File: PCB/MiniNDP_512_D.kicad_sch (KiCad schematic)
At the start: 17 parts, among them J1 Conn_02x20_Odd_Even, U1 HC138, U2 4040, U3 FCT821, U4 AS6C4008, U5 2G04, U6 1G32

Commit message: make E version default, easier to solder
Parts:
- added N1: MiniNDP_Cover, 000_LOCAL:MiniNDP_Cover, symbol 000_LOCAL:Housing
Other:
- note added: "TANDY 100/102/200 BUS -> Effect (A) ~{YO} A8 A9 A10 -> ~{BLOCK} ~{BYTE} Function L X X X X X X X H X X X X X X X L X X X X H L H L L -> L H Select BLOCK # from BANK 0 H L H L H -> L H Select BLOCK # from BANK 1 H L H H X -> H L Read or Write BYTE ~{BLOCK} L: sets A0-A9 to 0, updates A10-A18 from AD0-AD7 & BUS_A10 H: latches A10-A18 ~{BYTE} L: enables SRAM for read or write H: disables SRAM, incre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"
- note removed: "TANDY 100/102/200 BUS (A) ~{YO} A8 A9 A10 -> ~{BLOCK} ~{BYTE} L X X X X X X X H X X X X X X X L X X X X H L H L L -> L H Select BLOCK # from BANK0 H L H L H -> L H Select BLOCK # from BANK1 H L H H X -> H L READ/WRITE BYTE Each ~{BLOCK} pulse low: sets SRAM A0-A9 to 0 sets SRAM A10-A19 from BUS AD0-AD7 & A10 (AD0-AD7 = block#, BUS_A10 = bank#) On returning high: holds SRAM A10-A19 latched while h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"
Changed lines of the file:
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@@
 		)
 	)
-	(text "TANDY 100/102/200 BUS\n\n(A)	~{YO}   A8   A9  A10  ->  ~{BLOCK} ~{BYTE}\nL	X	X	X	X		X	  X\nX	H	X	X	X		X	  X\nX	X	L	X	X		X	  X\nH	L	H	L	L	->  L	  H  Select BLOCK # from BANK0\nH	L	H	L	H	->  L	  H  Select BLOCK # from BANK1\nH	L	H	H	X	->  H	  L  READ/WRITE BYTE\n\nEach ~{BLOCK} pulse low:\n  sets SRAM A0-A9 to 0\n  sets SRAM A10-A19 from BUS AD0-AD7 & A10\n  (AD0-AD7 = block#, BUS_A10 = bank#)\nOn returning high:\n  holds SRAM A10-A19 latched while high\n\nEach ~{BYTE} pulse low:\n  enables SRAM for read or write while low\nOn returning high:\n  disables SRAM\n  increments SRAM A0-A9 by 1\n"
-		(exclude_from_sim no)
-		(at 16.51 193.548 0)
-		(effects
-			(font
-				(face "KiCad Font")
-				(size 1 1)
-			)
-			(justify left bottom)
-		)
-	)
 	(text "3V"
 		(exclude_from_sim no)
@@
 		)
 	)
+	(text "TANDY 100/102/200 BUS  ->  Effect\n\n(A)	~{YO}   A8   A9  A10  ->  ~{BLOCK} ~{BYTE}    Function\nL	X	X	X	X		X	  X\nX	H	X	X	X		X	  X\nX	X	L	X	X		X	  X\nH	L	H	L	L	->  L	  H  Select BLOCK # from BANK 0\nH	L	H	L	H	->  L	  H  Select BLOCK # from BANK 1\nH	L	H	H	X	->  H	  L  Read or Write BYTE\n\n~{BLOCK}\nL: sets A0-A9 to 0, updates A10-A18 from AD0-AD7 & BUS_A10\nH: latches A10-A18\n\n~{BYTE}\nL: enables SRAM for read or write\nH: disables SRAM, increments A0-A9 by 1\n"
+		(exclude_from_sim no)
+		(at 18.288 191.77 0)
+		(effects
+			(font
+				(face "KiCad Font")
+				(size 1 1)
+			)
+			(justify left bottom)
+		)
+	)
 	(text "BUS_A12"
 		(exclude_from_sim no)
@@
 		)
 	)
-	(label "A2"
-		(at 636.27 17.78 0)
-		(fields_autoplaced yes)
-		(effects
-			(font
-				(size 1.27 1.27)
-			)
-			(justify left bottom)
-		)
-	)
 	(label "~{CE}"
 		(at 247.65 76.2 0)
@@
 		)
 	)
-	(label "A2"
-		(at 843.28 -5.08 0)
-		(fields_autoplaced yes)
-		(effects
-			(font
-				(size 1.27 1.27)
-			)
-			(justify left bottom)
-		)
-	)
 	(label "AD5"
 		(at 247.65 58.42 0)
@@
 		)
 	)
-	(label "A0"
-		(at 636.27 12.7 0)
-		(fields_autoplaced yes)
-		(effects
-			(font
-				(size 1.27 1.27)
-			)
-			(justify left bottom)
-		)
-	)
 	(label "A8"
 		(at 165.1 57.15 0)
@@
 		)
 	)
-	(label "A3"
-		(at 843.28 -2.54 0)
-		(fields_autoplaced yes)
-		(effects
-			(font
-				(size 1.27 1.27)
-			)
-			(justify left bottom)
-		)
-	)
-	(label "A4"
-		(at 604.52 12.7 0)
-		(fields_autoplaced yes)
-		(effects
-			(font
-				(size 1.27 1.27)
-			)
-			(justify left bottom)
-		)
-	)
 	(label "A1"
 		(at 165.1 39.37 0)
@@
 		)
 	)
-	(label "A1"
-		(at 636.27 15.24 0)
-		(fields_autoplaced yes)
-		(effects
-			(font
-				(size 1.27 1.27)
-			)
-			(justify left bottom)
-		)
-	)
 	(label "A4"
 		(at 165.1 46.99 0)
@@
 		)
 	)
-	(label "A6"
-		(at 604.52 17.78 0)
-		(fields_autoplaced yes)
-		(effects
-			(font
-				(size 1.27 1.27)
-			)
-			(justify left bottom)
-		)
-	)
 	(label "A9"
 		(at 165.1 59.69 0)
@@
 		)
 	)
-	(label "A1"
-		(at 843.28 -7.62 0)
-		(fields_autoplaced yes)
-		(effects
-			(font
-				(size 1.27 1.27)
-			)
-			(justify left bottom)
-		)
-	)
-	(label "A3"
-		(at 636.27 20.32 0)
-		(fields_autoplaced yes)
-		(effects
-			(font
-				(size 1.27 1.27)
-			)
-			(justify left bottom)
-		)
-	)
 	(label "AD4"
 		(at 139.7 110.49 180)
@@
 		)
 	)
-	(label "A5"
-		(at 604.52 15.24 0)
-		(fields_autoplaced yes)
-		(effects
-			(font
-				(size 1.27 1.27)
-			)
-			(justify left bottom)
-		)
-	)
 	(label "A3"
 		(at 165.1 44.45 0)
@@
 		)
 	)
-	(label "A7"
-		(at 604.52 20.32 0)
-		(fields_autoplaced yes)
-		(effects
-			(font
-				(size 1.27 1.27)
-			)
-			(justify left bottom)
-		)
-	)
 	(label "{BUS_A[8..9],(A),~{Y0}}"
 		(at 46.99 69.85 0)
@@
 		)
 	)
-	(label "A0"
-		(at 843.28 -10.16 0)
-		(fields_autoplaced yes)
-		(effects
-			(font
-				(size 1.27 1.27)
-			)
-			(justify left bottom)
-		)
-	)
 	(label "AD4"
 		(at 50.8 95.25 180)
@@
 					(unit 1)
 				)
+			)
+		)
+	)
+	(symbol
+		(lib_id "000_LOCAL:Housing")
+		(at 234.95 29.21 0)
+		(unit 1)
+		(exclude_from_sim yes)
+		(in_bom no)
+		(on_board yes)
+		(dnp no)
+		(fields_autoplaced yes)
+		(property "Reference" "N1"
+			(at 238.76 28.2574 0)
+			(effects
+				(font
+					(size 1.27 1.27)
+				)
+				(justify left)
+			)
+		)
+		(property "Value" "MiniNDP_Cover"
+			(at 238.76 30.7974 0)
+			(effects
+				(font
+					(size 1.27 1.27)
+				)
+				(justify left)
+			)
+		)
+		(property "Footprint" "000_LOCAL:MiniNDP_Cover"
+			(at 236.22 27.94 0)
+			(effects
+				(font
+					(size 1.27 1.27)
+				)
+				(hide yes)
+			)
+		)
+		(property "Datasheet" "../COVER/MiniNDP_Cover.scad"
+			(at 236.22 27.94 0)
+			(effects
+				(font
+					(size 1.27 1.27)
+				)
+				(hide yes)
+			)
+		)
+		(property "Description" "Snap cover for MiniNDP"
+			(at 234.95 29.21 0)
+			(effects
+				(font
+					(size 1.27 1.27)
+				)
+				(hide yes)
+			)
+		)
+		(property "MPN" "MiniNDP_Cover.stl"
+			(at 234.95 29.21 0)
+			(effects
+				(font
+					(size 1.27 1.27)
+				)
+				(hide yes)
+			)
+		)
+		(instances
+			(project "MiniNDP_512_D"
+				(path "/f15c2929-5cf4-4b4e-965d-148e1bec8a42"
+					(reference "N1")
+					(unit 1)
+				)

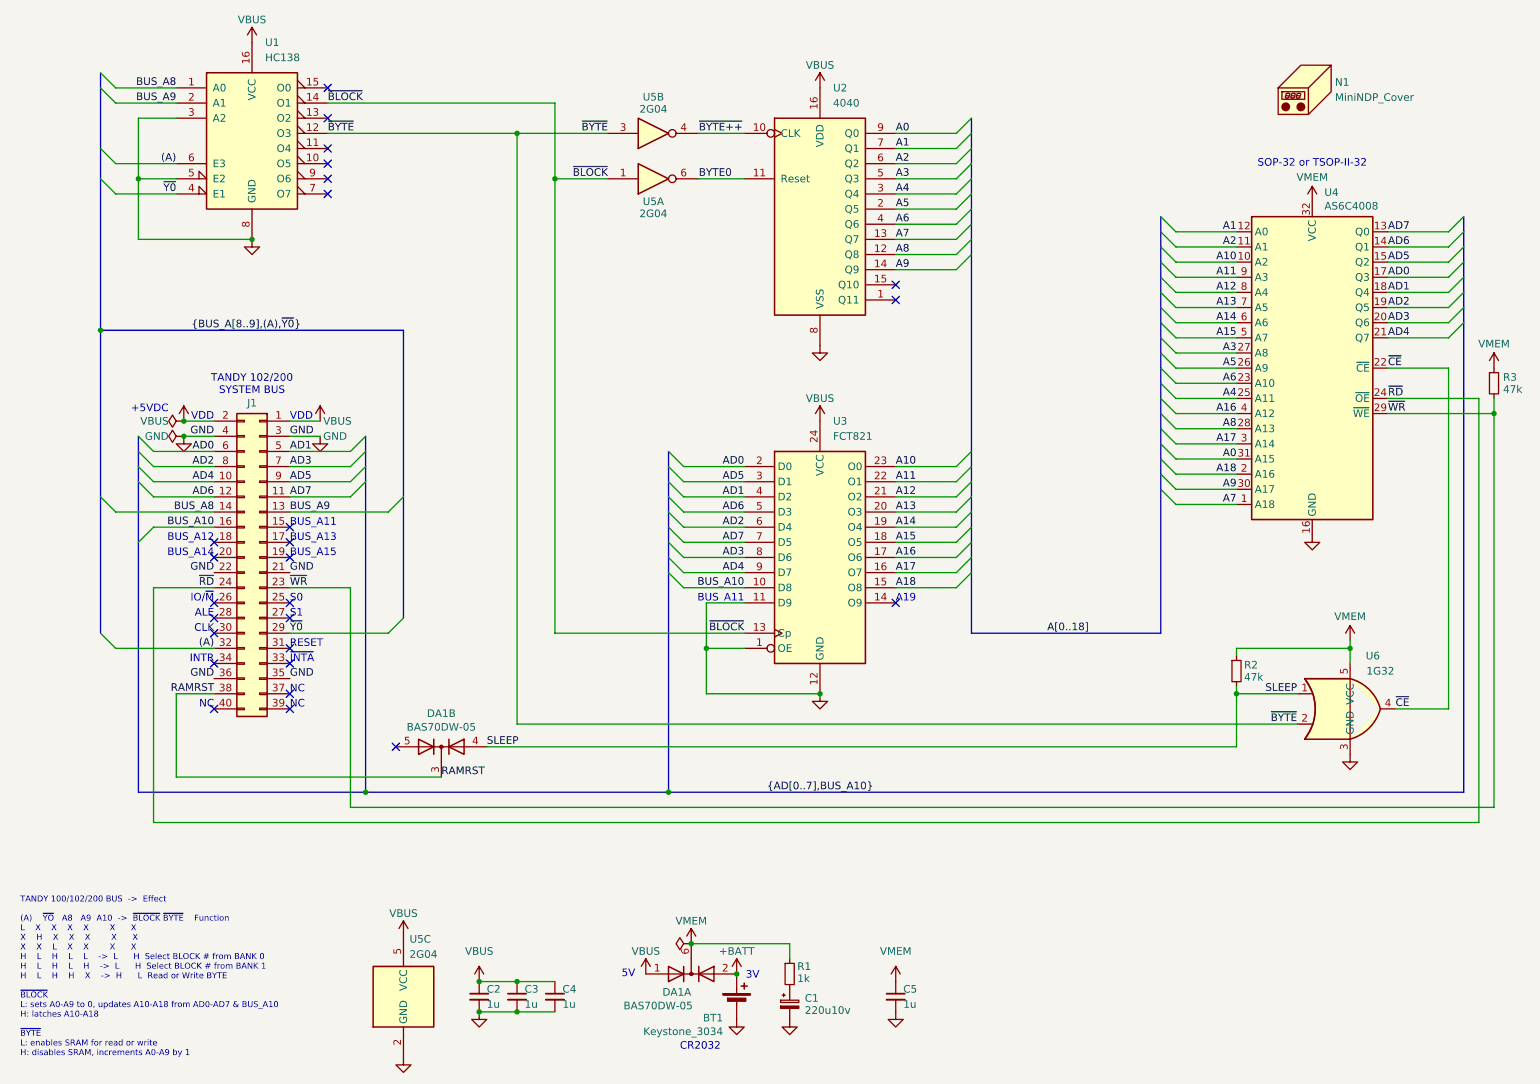
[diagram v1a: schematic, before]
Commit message: larger parts on D version and proper bom
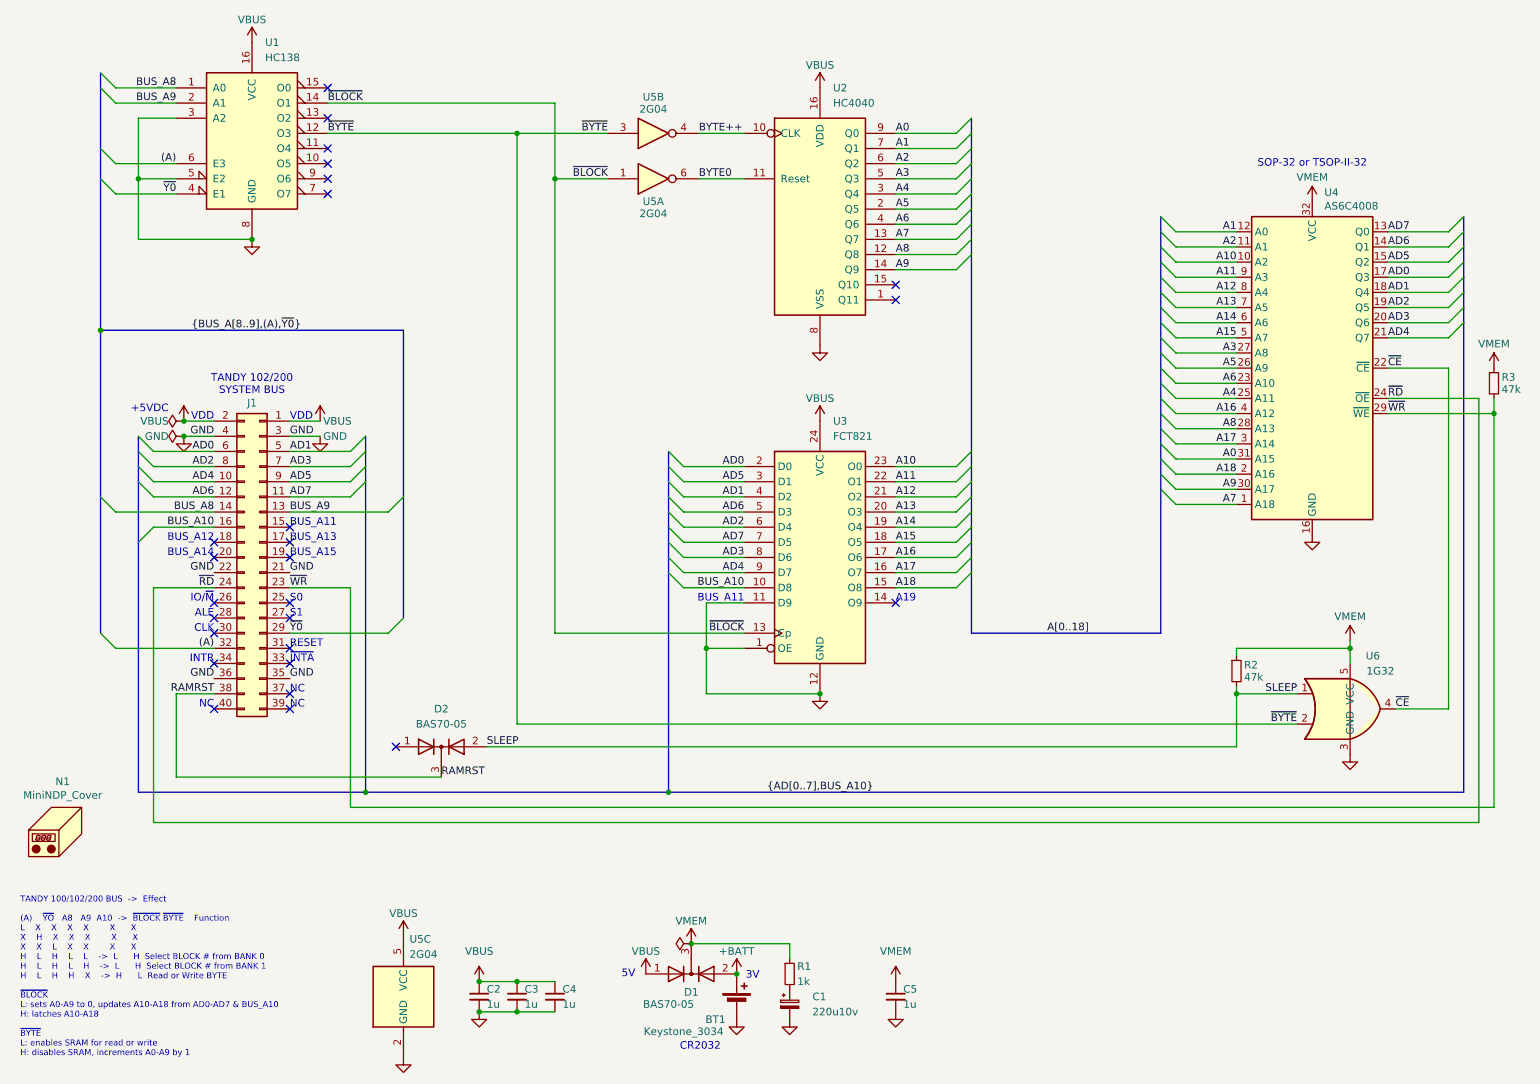
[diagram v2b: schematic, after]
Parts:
- removed DA1: BAS70DW-05, 000_LOCAL:SOT-363_SC-70-6_symmetric, symbol 000_LOCAL:BAV70S
- added D1, D2: BAS70-05, 000_LOCAL:SOT-23, symbol 000_LOCAL:BAV70
- BT1: MPN (none) -> Keystone 3034
- C1: MPN (none) -> TAJC227K010RNJ
- C2, C3, C4, C5: MPN (none) -> CL21B105KAFNNNE
- J1: MPN (none) -> 302-S401
- R1: MPN (none) -> RK73B2ATTD102J
- R2, R3: MPN (none) -> RMCF0805FT47K0
- U1: MPN (none) -> 74AHC138D,118
- U2: value 4040 -> HC4040; MPN (none) -> IC BINARY COUNTER 12-BIT 16SO
- U3: MPN (none) -> CY74FCT821BTSOC
- U4: MPN (none) -> AS6C4008-55ZIN
- U5: footprint 000_LOCAL:SOT-363_SC-70-6 -> 000_LOCAL:TSOP-6_1.65x3.05mm_P0.95mm; MPN (none) -> 74HC2G04GW,125
- U6: footprint 000_LOCAL:SOT-353_SC-70-5 -> 000_LOCAL:SOT-23-5; MPN (none) -> SN74AHC1G32DBVR
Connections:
- net +BATT: now also D1.2 (A)
- net RAMRST: now also D2.3 (K)
- net SLEEP: now also D2.2 (A)
- net VBUS: now also D1.1 (A)
- net VMEM: now also D1.3 (K)
- net ~{BYTE++} renamed BYTE++
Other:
- moved on the sheet: N1
